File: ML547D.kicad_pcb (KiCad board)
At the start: 2 copper layers, 100 x 36 mm, 0 parts

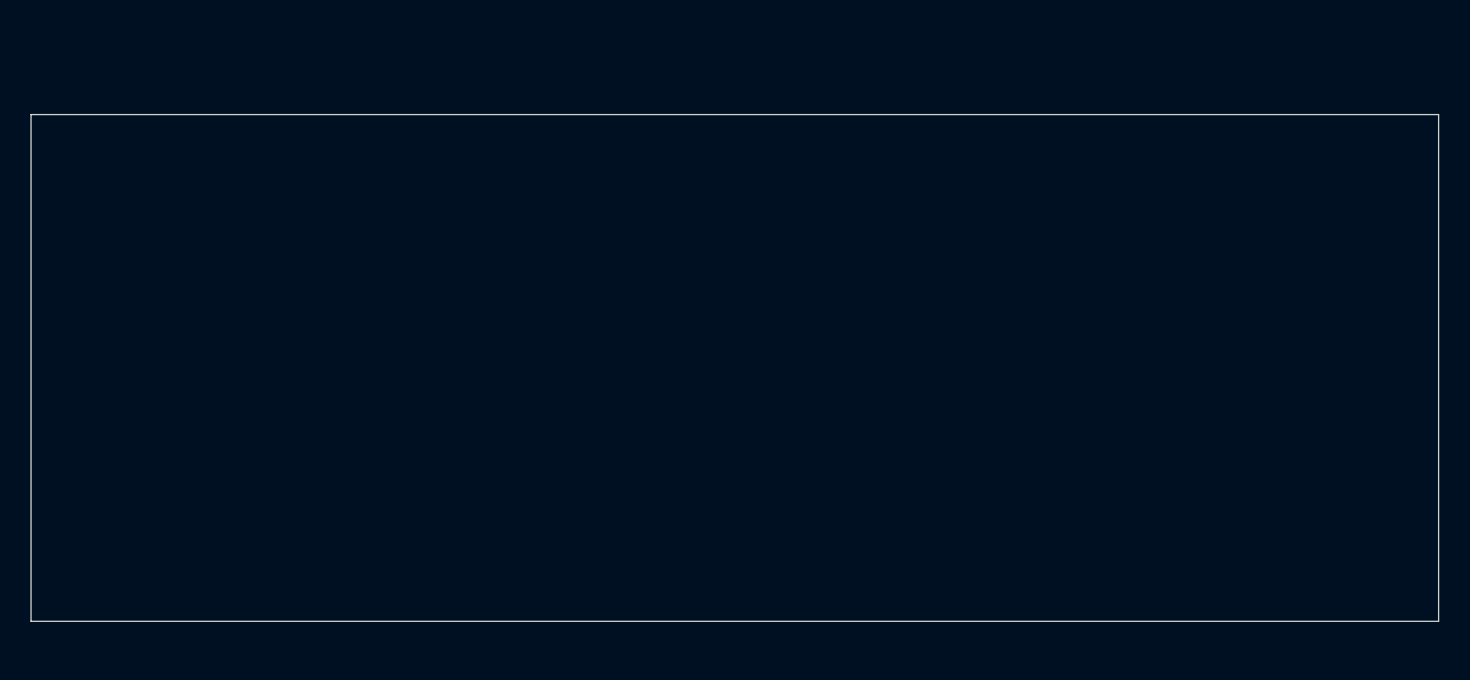
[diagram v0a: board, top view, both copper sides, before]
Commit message: full wiring, shield guards missing
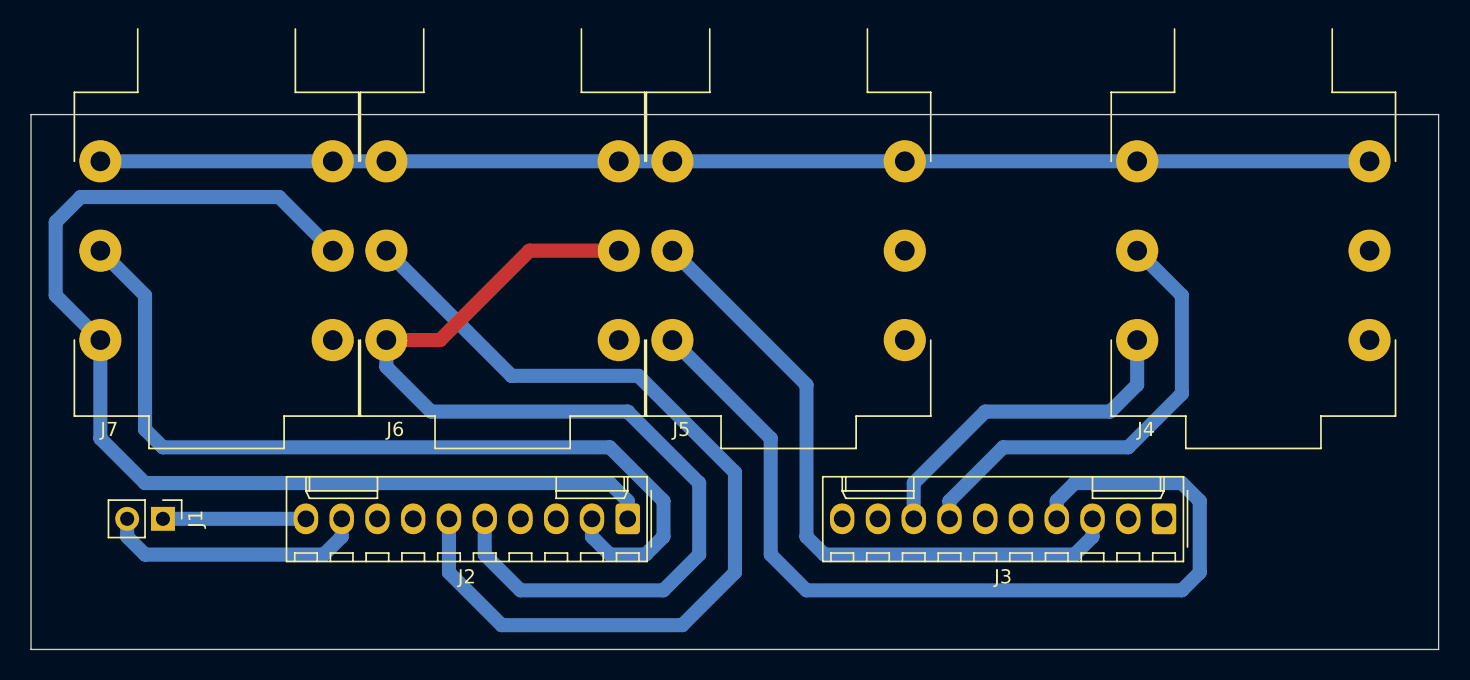
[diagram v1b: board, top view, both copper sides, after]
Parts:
- added J1: Direct Out, Connector_PinHeader_2.54mm:PinHeader_1x02_P2.54mm_Vertical, F.Cu at (39.4, 172.7)
- added J2: Ribbon, Connector_Molex:Molex_KK-254_AE-6410-10A_1x10_P2.54mm_Vertical, F.Cu at (72.4, 172.7)
- added J3: Ribbon, Connector_Molex:Molex_KK-254_AE-6410-10A_1x10_P2.54mm_Vertical, F.Cu at (110.5, 172.7)
- added J4: Input R, Cliff:CL13345, F.Cu at (116.8, 147.3)
- added J5: Input L, Cliff:CL13345, F.Cu at (83.8, 147.3)
- added J6: Insert R, Cliff:CL13345, F.Cu at (63.5, 147.3)
- added J7: Insert L, Cliff:CL13345, F.Cu at (43.2, 147.3)
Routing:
- net Net-(J4-PadS): track 0.00 -> 90.2 mm
- net Net-(J2-Pad1): track 0.00 -> 79.3 mm
- net Net-(J2-Pad5): track 0.00 -> 71.7 mm
- net Net-(J3-Pad4): track 0.00 -> 67.8 mm
- net Net-(J2-Pad6): track 0.00 -> 65.6 mm
- net Net-(J2-Pad2): track 0.00 -> 62.9 mm
- net Net-(J3-Pad3): track 0.00 -> 46.9 mm
- net Net-(J3-Pad7): track 0.00 -> 32.4 mm
- net Net-(J3-Pad8): track 0.00 -> 24.5 mm
- net Net-(J1-Pad2): track 0.00 -> 18.8 mm
- net Net-(J1-Pad1): track 0.00 -> 10.2 mm
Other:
- board size 100 x 36 mm -> 100 x 38 mm

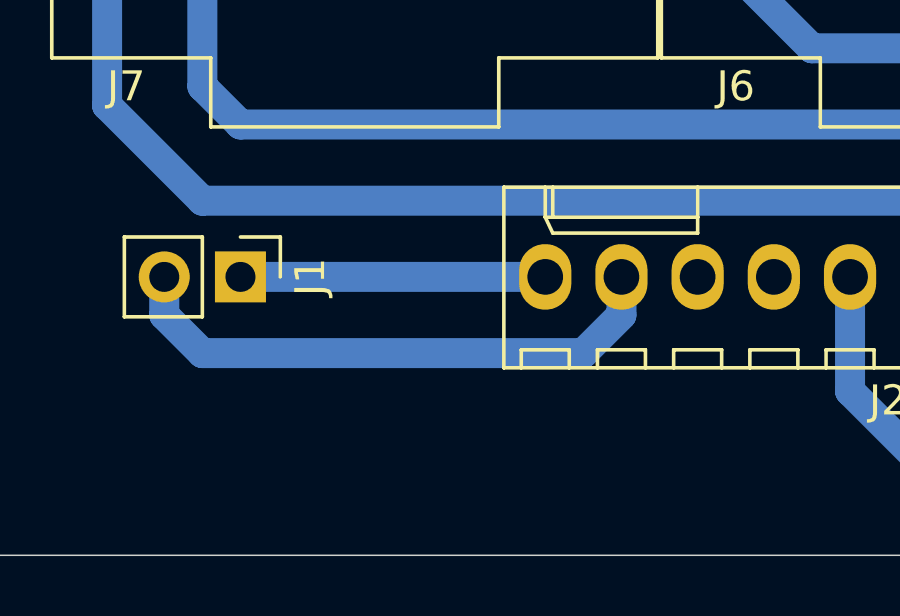
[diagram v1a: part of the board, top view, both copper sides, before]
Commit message: fixed direct out wiring
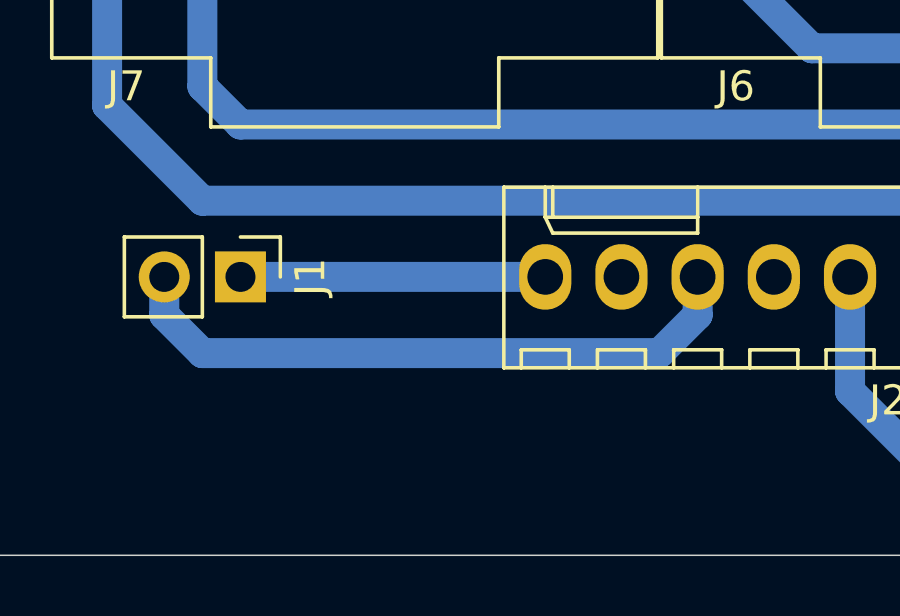
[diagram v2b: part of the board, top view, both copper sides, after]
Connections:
- J2 pad 8: Net-(J2-Pad8) -> Net-(J1-Pad2)
- J2 pad 9: Net-(J1-Pad2) -> Net-(J2-Pad9)
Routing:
- net Net-(J1-Pad2): track 18.8 -> 21.4 mm

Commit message: updated direct out to 3 pin header
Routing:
- net Net-(J2-Pad9): track 0.00 -> 0.63 mm
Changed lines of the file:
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@@
     (thickness 1.6)
     (drawings 4)
-    (tracks 80)
+    (tracks 81)
     (zones 0)
     (modules 7)
@@
   )
   (setup
-    (last_trace_width 1)
+    (last_trace_width 0.25)
     (user_trace_width 1)
     (user_trace_width 4)
@@
   (segment (start 92.075 147.32) (end 108.585 147.32) (width 1) (layer B.Cu) (net 20))
   (segment (start 108.585 147.32) (end 125.095 147.32) (width 1) (layer B.Cu) (net 20))
+  (segment (start 52.07 172.72) (end 52.07 173.355) (width 0.25) (layer B.Cu) (net 27))
 )

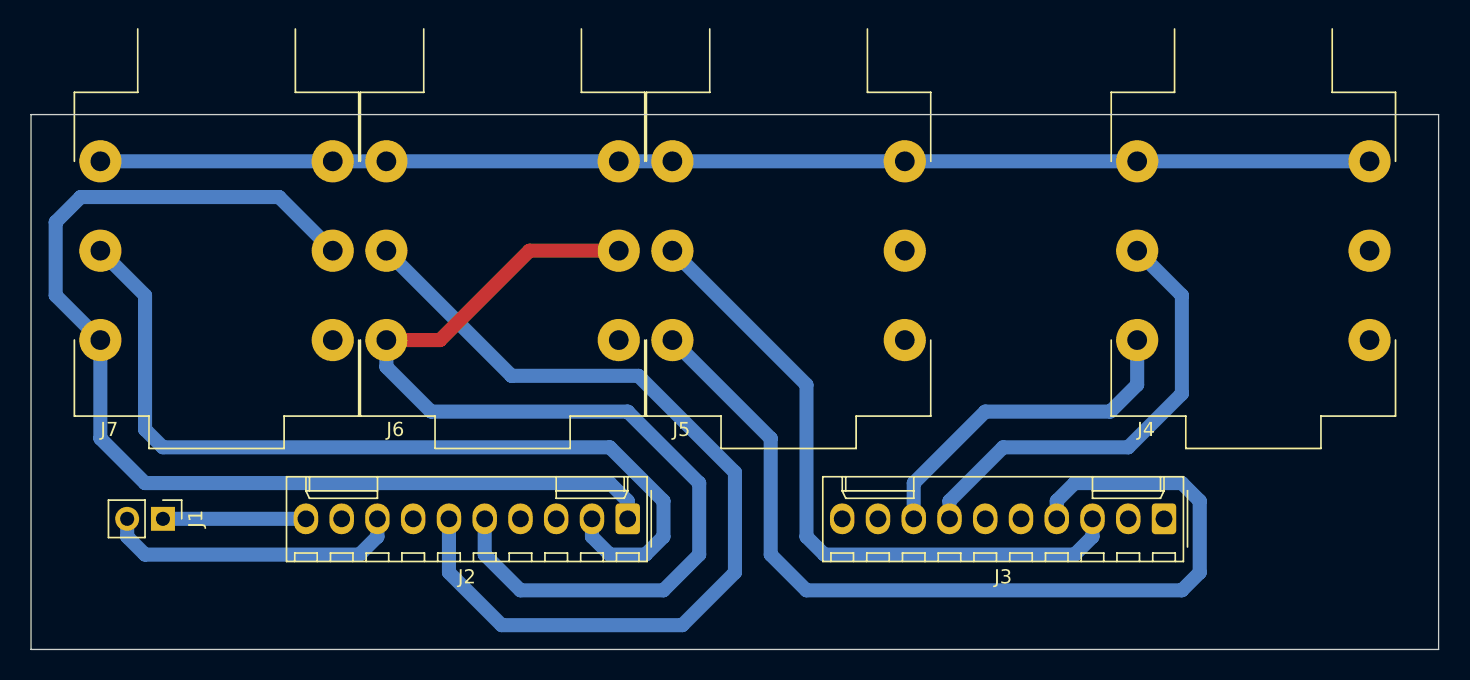
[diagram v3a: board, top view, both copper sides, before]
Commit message: added shield guards
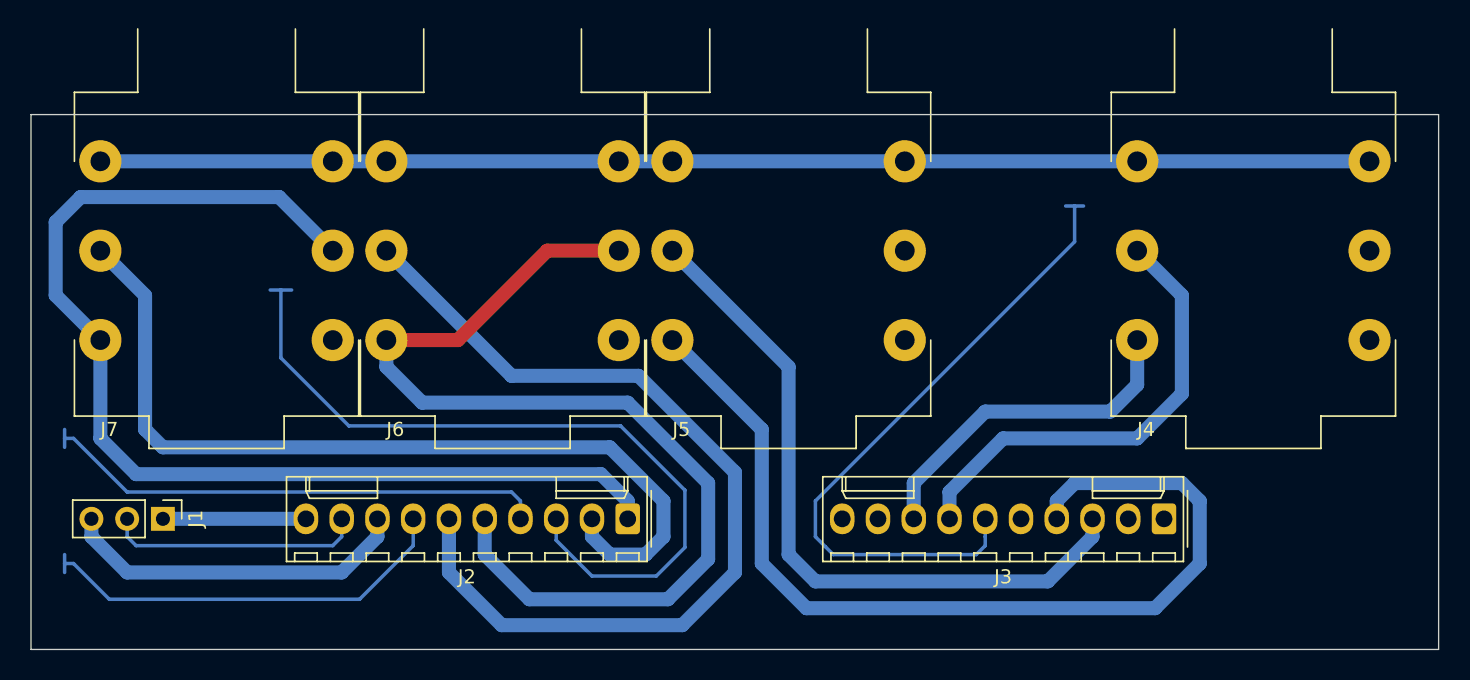
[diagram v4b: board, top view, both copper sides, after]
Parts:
- J1: footprint Connector_PinHeader_2.54mm:PinHeader_1x02_P2.54mm_Vertical -> Connector_PinHeader_2.54mm:PinHeader_1x03_P2.54mm_Vertical
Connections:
- J2 pad 8: Net-(J1-Pad2) -> Net-(J1-Pad3)
- J2 pad 9: Net-(J2-Pad9) -> Net-(J1-Pad2)
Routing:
- net Net-(J2-Pad3): track 0.00 -> 55.6 mm
- net Net-(J3-Pad6): track 0.00 -> 47.2 mm
- net Net-(J2-Pad4): track 0.00 -> 36.8 mm
- net Net-(J2-Pad7): track 0.00 -> 30.6 mm
- net Net-(J1-Pad3): track 0.00 -> 25.0 mm
- net Net-(J3-Pad3): track 46.9 -> 50.0 mm
- net Net-(J1-Pad2): track 21.4 -> 18.9 mm
- net Net-(J2-Pad5): track 71.7 -> 73.6 mm
- net Net-(J3-Pad4): track 67.8 -> 69.2 mm
- net Net-(J2-Pad9): track 0.63 -> 0.00 mm

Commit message: adden copper fill on imperial grid
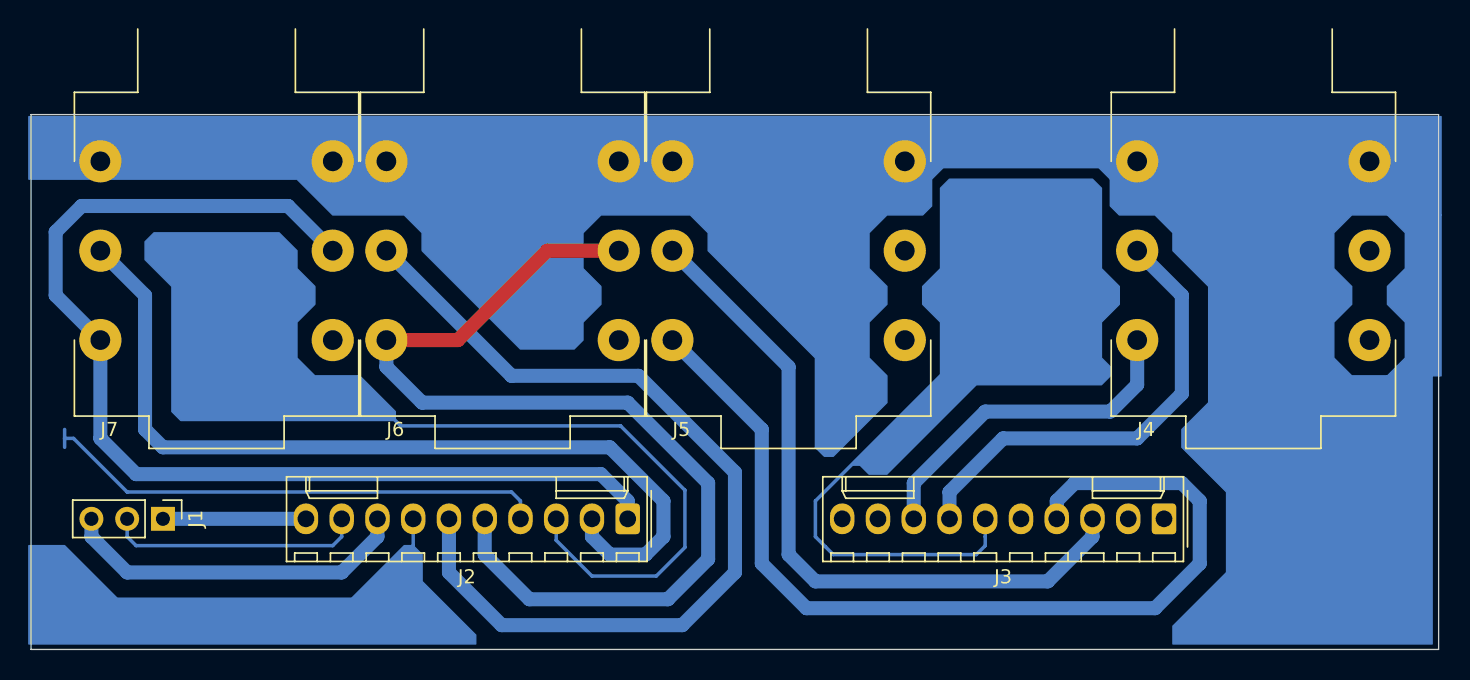
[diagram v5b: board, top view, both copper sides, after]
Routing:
- net Net-(J2-Pad1): track 79.3 -> 78.3 mm

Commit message: added name tag to copper
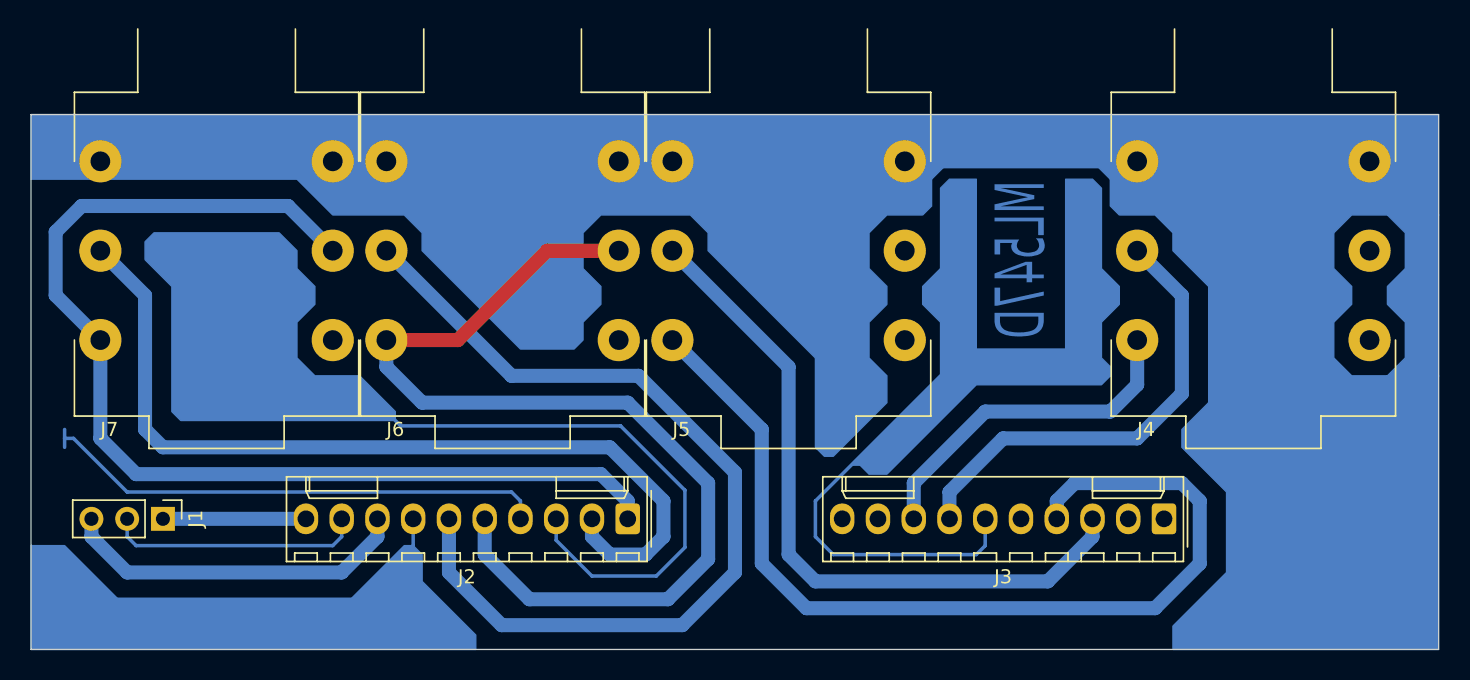
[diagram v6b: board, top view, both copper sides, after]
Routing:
- net Net-(J3-Pad6): track 47.2 -> 29.9 mm
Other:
- board text added: "ML547D"

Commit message: reversed pinorder of J2 and J3 with project library footprint
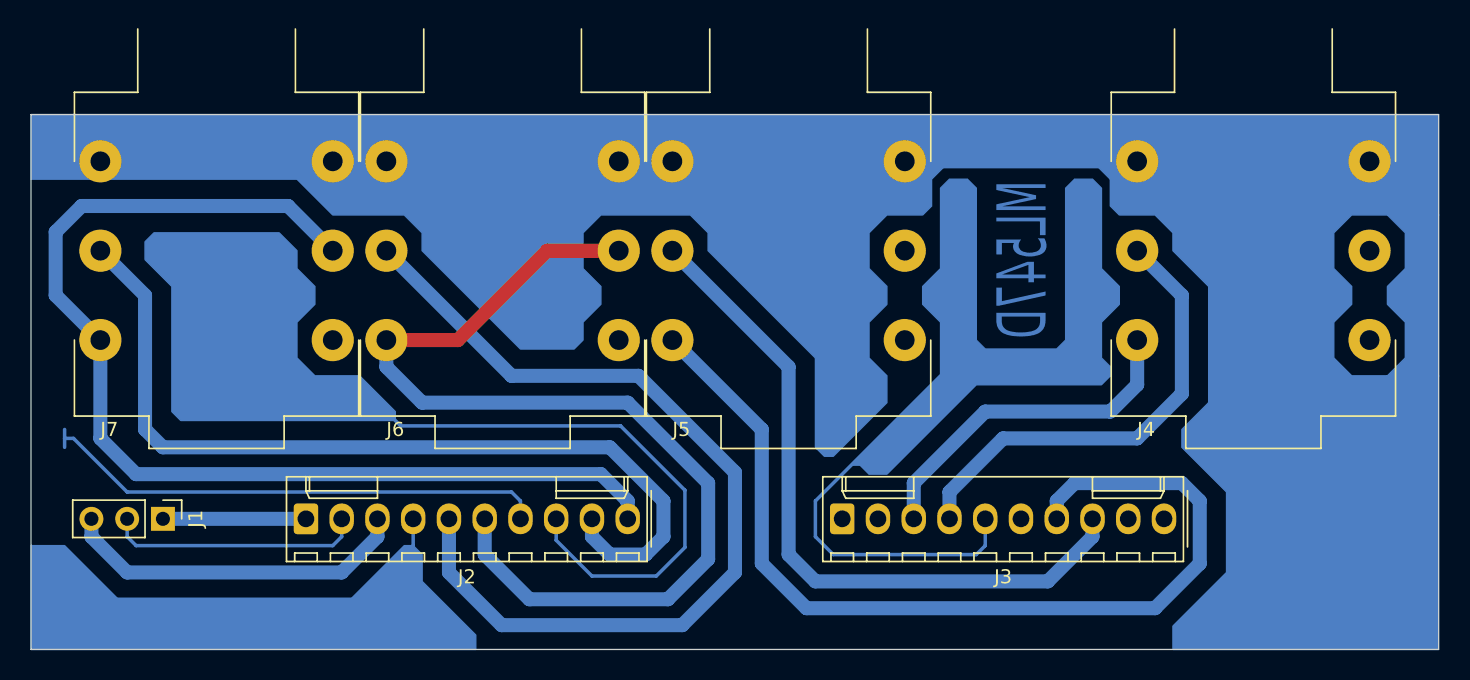
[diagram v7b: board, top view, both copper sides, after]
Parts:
- J2, J3: footprint Connector_Molex:Molex_KK-254_AE-6410-10A_1x10_P2.54mm_Vertical -> ML547D:Molex_KK-254_AE-6410-10A_1x10_P2.54mm_Vertical_reversed
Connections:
- J2 pad 1: Net-(J2-Pad1) -> Net-(J1-Pad1)
- J2 pad 10: Net-(J1-Pad1) -> Net-(J2-Pad10)
- J2 pad 2: Net-(J2-Pad2) -> Net-(J1-Pad2)
- J2 pad 3: Net-(J2-Pad3) -> Net-(J1-Pad3)
- J2 pad 8: Net-(J1-Pad3) -> Net-(J2-Pad8)
- J2 pad 9: Net-(J1-Pad2) -> Net-(J2-Pad9)
- J4 pad R: Net-(J3-Pad7) -> Net-(J3-Pad4)
- J4 pad T: Net-(J3-Pad8) -> Net-(J3-Pad3)
- J5 pad R: Net-(J3-Pad3) -> Net-(J3-Pad8)
- J5 pad T: Net-(J3-Pad4) -> Net-(J3-Pad7)
- J6 pad R: Net-(J2-Pad6) -> Net-(J2-Pad5)
- J6 pad RN: Net-(J2-Pad5) -> Net-(J2-Pad6)
- J6 pad T: Net-(J2-Pad5) -> Net-(J2-Pad6)
- J7 pad R: Net-(J2-Pad2) -> Net-(J2-Pad9)
- J7 pad RN: Net-(J2-Pad1) -> Net-(J2-Pad10)
- J7 pad T: Net-(J2-Pad1) -> Net-(J2-Pad10)
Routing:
- net Net-(J2-Pad10): track 0.00 -> 78.3 mm
- net Net-(J2-Pad1): track 78.3 -> 0.00 mm
- net Net-(J2-Pad9): track 0.00 -> 62.9 mm
- net Net-(J2-Pad2): track 62.9 -> 0.00 mm
- net Net-(J2-Pad8): track 0.00 -> 55.6 mm
- net Net-(J2-Pad3): track 55.6 -> 0.00 mm
- net Net-(J3-Pad7): track 32.8 -> 69.2 mm
- net Net-(J3-Pad4): track 69.2 -> 32.8 mm
- net Net-(J3-Pad6): track 29.9 -> 0.00 mm
- net Net-(J3-Pad5): track 0.00 -> 29.9 mm
- net Net-(J3-Pad8): track 24.5 -> 50.0 mm
- net Net-(J3-Pad3): track 50.0 -> 24.5 mm
- net Net-(J2-Pad6): track 65.6 -> 73.6 mm
- net Net-(J2-Pad5): track 73.6 -> 65.6 mm
- net Net-(J2-Pad7): track 30.6 -> 36.8 mm
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
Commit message: prepare adding lib submodule
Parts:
- J2, J3: footprint ML547D:Molex_KK-254_AE-6410-10A_1x10_P2.54mm_Vertical_reversed -> TAC:Molex_KK-254_AE-6410-10A_1x10_P2.54mm_Vertical_reversed
- J4, J5, J6, J7: footprint Cliff:CL13345 -> TAC:CL13345
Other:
- board text added: "v1.0"
